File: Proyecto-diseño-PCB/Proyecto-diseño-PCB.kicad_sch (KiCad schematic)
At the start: 41 parts, among them J1 USB_B_Micro, J2 PROGRAMACIÓN/DEPURACIÓN, J3 LADO A, J4 LADO B, SW1 BOTON, SW2 BOTON, SW3 RESET, U1 TPD2EUSB30, U2 LP2950-3.3_TO92, U3 PIC18LF45K50-I/P

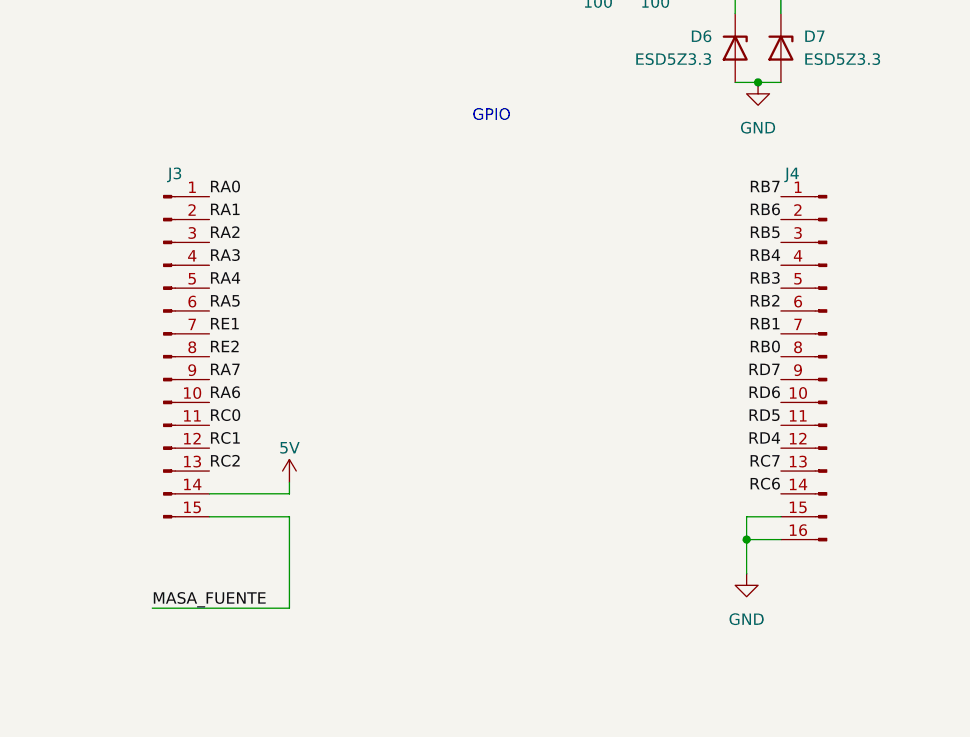
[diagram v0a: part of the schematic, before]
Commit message: Di vuelta pines para que el 1 (cuadrado) sea tierra
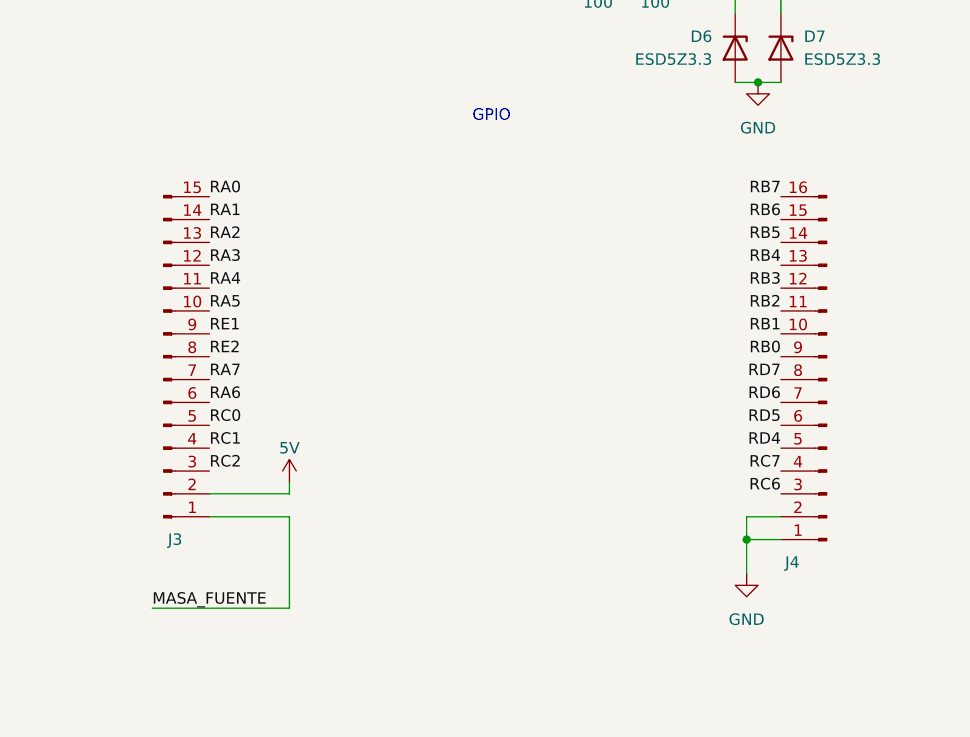
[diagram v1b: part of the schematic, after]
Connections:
- net 5V: now also J3.2 (Pin_2); no longer J3.14 (Pin_14)
- net GND: now also J4.1 (Pin_1), J4.2 (Pin_2); no longer J4.15 (Pin_15), J4.16 (Pin_16)
- net MASA_FUENTE: now also J3.1 (Pin_1); no longer J3.15 (Pin_15)
- net RA0: now also J3.15 (Pin_15); no longer J3.1 (Pin_1)
- net RA1: now also J3.14 (Pin_14); no longer J3.2 (Pin_2)
- net RA2: now also J3.13 (Pin_13); no longer J3.3 (Pin_3)
- net RA3: now also J3.12 (Pin_12); no longer J3.4 (Pin_4)
- net RA4: now also J3.11 (Pin_11); no longer J3.5 (Pin_5)
- net RA5: now also J3.10 (Pin_10); no longer J3.6 (Pin_6)
- net RA6: now also J3.6 (Pin_6); no longer J3.10 (Pin_10)
- net RA7: now also J3.7 (Pin_7); no longer J3.9 (Pin_9)
- net RB0: now also J4.9 (Pin_9); no longer J4.8 (Pin_8)
- net RB1: now also J4.10 (Pin_10); no longer J4.7 (Pin_7)
- net RB2: now also J4.11 (Pin_11); no longer J4.6 (Pin_6)
- net RB3: now also J4.12 (Pin_12); no longer J4.5 (Pin_5)
- net RB4: now also J4.13 (Pin_13); no longer J4.4 (Pin_4)
- net RB5: now also J4.14 (Pin_14); no longer J4.3 (Pin_3)
- net RB6: now also J4.15 (Pin_15); no longer J4.2 (Pin_2)
- net RB7: now also J4.16 (Pin_16); no longer J4.1 (Pin_1)
- net RC0: now also J3.5 (Pin_5); no longer J3.11 (Pin_11)
- net RC1: now also J3.4 (Pin_4); no longer J3.12 (Pin_12)
- net RC2: now also J3.3 (Pin_3); no longer J3.13 (Pin_13)
- net RC6: now also J4.3 (Pin_3); no longer J4.14 (Pin_14)
- net RC7: now also J4.4 (Pin_4); no longer J4.13 (Pin_13)
- net RD4: now also J4.5 (Pin_5); no longer J4.12 (Pin_12)
- net RD5: now also J4.6 (Pin_6); no longer J4.11 (Pin_11)
- net RD6: now also J4.7 (Pin_7); no longer J4.10 (Pin_10)
- net RD7: now also J4.8 (Pin_8); no longer J4.9 (Pin_9)
- net RE1: now also J3.9 (Pin_9); no longer J3.7 (Pin_7)
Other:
- moved on the sheet: J4
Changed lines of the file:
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@@
 	(symbol
 		(lib_id "Connector:Conn_01x16_Pin")
-		(at 270.51 119.38 0)
-		(mirror y)
+		(at 270.51 121.92 180)
 		(unit 1)
 		(exclude_from_sim no)
@@
 		(dnp no)
 		(property "Reference" "J4"
-			(at 266.7 99.06 0)
+			(at 266.7 142.24 0)
 			(effects
 				(font
@@
 		)
 		(property "Value" "LADO B"
-			(at 271.78 120.6499 0)
+			(at 271.78 120.6501 0)
 			(effects
 				(font
@@
 		)
 		(property "Footprint" "Connector_PinHeader_2.54mm:PinHeader_1x16_P2.54mm_Vertical"
-			(at 270.51 119.38 0)
+			(at 270.51 121.92 0)
 			(effects
 				(font
@@
 		)
 		(property "Datasheet" "~"
-			(at 270.51 119.38 0)
+			(at 270.51 121.92 0)
 			(effects
 				(font
@@
 		)
 		(property "Description" "Generic connector, single row, 01x16, script generated"
-			(at 270.51 119.38 0)
+			(at 270.51 121.92 0)
 			(effects
 				(font
@@
 		(lib_id "Connector:Conn_01x15_Pin")
 		(at 196.85 119.38 0)
+		(mirror x)
 		(unit 1)
 		(exclude_from_sim no)
@@
 		(dnp no)
 		(property "Reference" "J3"
-			(at 198.12 99.06 0)
+			(at 198.12 139.7 0)
 			(effects
 				(font
@@
 		)
 		(property "Value" "LADO A"
-			(at 197.485 101.6 0)
-			(effects
-				(font
+			(at 197.485 137.16 0)
+			(effects
+				(font

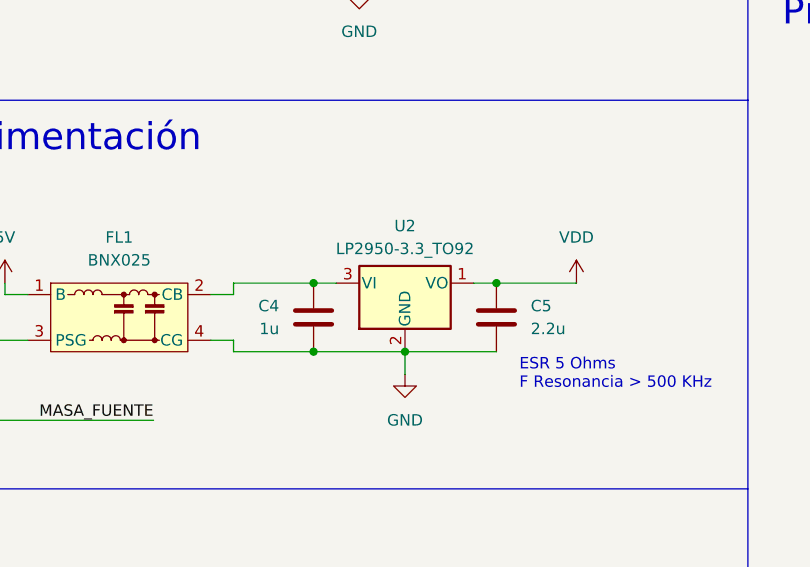
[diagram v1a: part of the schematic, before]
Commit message: Cambié algunos footprints y componentes
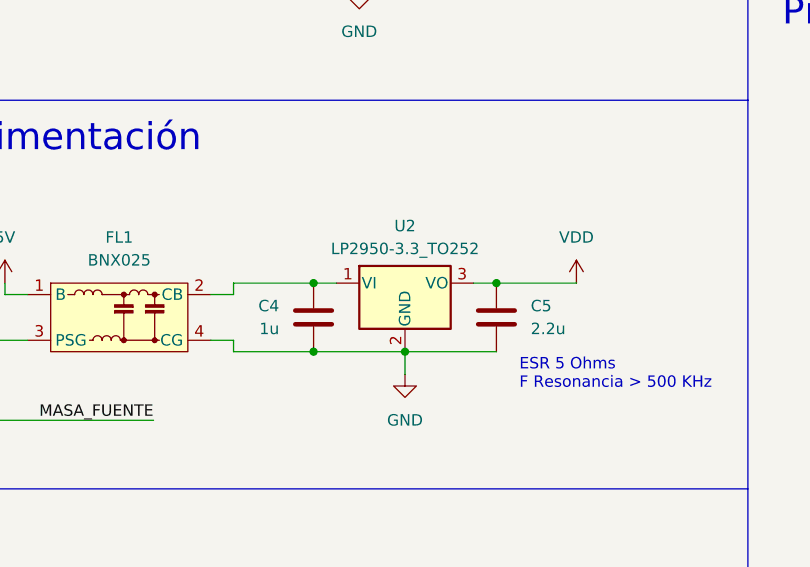
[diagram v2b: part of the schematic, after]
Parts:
- J2: footprint Connector_PinHeader_2.54mm:PinHeader_1x05_P2.54mm_Vertical -> Connector_PinSocket_2.54mm:PinSocket_1x05_P2.54mm_Vertical
- J3: footprint Connector_PinHeader_2.54mm:PinHeader_1x15_P2.54mm_Vertical -> Connector_PinSocket_2.54mm:PinSocket_1x15_P2.54mm_Vertical
- J4: footprint Connector_PinHeader_2.54mm:PinHeader_1x16_P2.54mm_Vertical -> Connector_PinSocket_2.54mm:PinSocket_1x16_P2.54mm_Vertical
- SW3: footprint Button_Switch_THT:SW_PUSH_6mm -> Button_Switch_THT:SW_Tactile_SPST_Angled_PTS645Vx31-2LFS
- U2: value LP2950-3.3_TO92 -> LP2950-3.3_TO252; footprint Package_TO_SOT_THT:TO-92_Inline -> Package_TO_SOT_SMD:TO-252-2; symbol Regulator_Linear:LP2950-3.3_TO92 -> Regulator_Linear:LP2950-3.3_TO252
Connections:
- net VDD: now also U2.3 (VO); no longer U2.1 (VO)
- net at C4.2, FL1.2 (CB): now also U2.1 (VI); no longer U2.3 (VI)
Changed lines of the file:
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@@
 			)
 		)
-		(property "Footprint" "Connector_PinHeader_2.54mm:PinHeader_1x05_P2.54mm_Vertical"
+		(property "Footprint" "Connector_PinSocket_2.54mm:PinSocket_1x05_P2.54mm_Vertical"
 			(at 236.22 69.85 0)
 			(effects
@@
 			)
 		)
-		(property "Footprint" "Button_Switch_THT:SW_PUSH_6mm"
+		(property "Footprint" "Button_Switch_THT:SW_Tactile_SPST_Angled_PTS645Vx31-2LFS"
 			(at 25.4 44.45 0)
 			(effects
@@
 			)
 		)
-		(property "Footprint" "Connector_PinHeader_2.54mm:PinHeader_1x16_P2.54mm_Vertical"
+		(property "Footprint" "Connector_PinSocket_2.54mm:PinSocket_1x16_P2.54mm_Vertical"
 			(at 270.51 121.92 0)
 			(effects
@@
 	)
 	(symbol
-		(lib_id "Regulator_Linear:LP2950-3.3_TO92")
+		(lib_id "Regulator_Linear:LP2950-3.3_TO252")
 		(at 139.7 87.63 0)
 		(unit 1)
@@
 			)
 		)
-		(property "Value" "LP2950-3.3_TO92"
+		(property "Value" "LP2950-3.3_TO252"
 			(at 139.7 83.82 0)
 			(effects
@@
 			)
 		)
-		(property "Footprint" "Package_TO_SOT_THT:TO-92_Inline"
+		(property "Footprint" "Package_TO_SOT_SMD:TO-252-2"
 			(at 139.7 81.915 0)
 			(effects
@@
 			)
 		)
-		(property "Description" "Positive 100mA 30V Linear Micropower Voltage Regulator, Fixed Output 3.3V, TO-92"
+		(property "Description" "Positive 100mA 30V Linear Micropower Voltage Regulator, Fixed Output 3.3V, TO-252"
 			(at 139.7 87.63 0)
 			(effects
@@
 			)
 		)
-		(property "Footprint" "Connector_PinHeader_2.54mm:PinHeader_1x15_P2.54mm_Vertical"
+		(property "Footprint" "Connector_PinSocket_2.54mm:PinSocket_1x15_P2.54mm_Vertical"
 			(at 196.85 119.38 0)
 			(effects

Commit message: rest of the f-ing owl
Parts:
- C1, C2, C3, C4, C5, C6, C7, C8: footprint Capacitor_THT:C_Disc_D3.4mm_W2.1mm_P2.50mm -> Capacitor_SMD:C_1206_3216Metric_Pad1.33x1.80mm_HandSolder
- J3: footprint Connector_PinSocket_2.54mm:PinSocket_1x15_P2.54mm_Vertical -> Connector_PinSocket_2.54mm:PinSocket_1x16_P2.54mm_Vertical; symbol Connector:Conn_01x15_Pin -> Connector:Conn_01x16_Pin
- J4: footprint Connector_PinSocket_2.54mm:PinSocket_1x16_P2.54mm_Vertical -> Connector_PinSocket_2.54mm:PinSocket_1x14_P2.54mm_Vertical; symbol Connector:Conn_01x16_Pin -> Connector:Conn_01x14_Pin
- R1, R10, R11, R12, R13, R2, R3, R4, R5, R6, R7, R8, R9: footprint Resistor_THT:R_Axial_DIN0204_L3.6mm_D1.6mm_P5.08mm_Horizontal -> Resistor_SMD:R_1206_3216Metric_Pad1.30x1.75mm_HandSolder
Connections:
- net BOTON1: now also U3.19 (RD0); no longer U3.22 (RD3)
- net BOTON2: now also U3.20 (RD1); no longer U3.21 (RD2)
- net LED_ROJO: now also U3.22 (RD3); no longer U3.19 (RD0)
- net LED_VERDE: now also U3.21 (RD2); no longer U3.20 (RD1)
- net RA0: now also J3.16 (Pin_16); no longer J3.15 (Pin_15)
- net RA1: now also J3.15 (Pin_15); no longer J3.14 (Pin_14)
- net RA2: now also J3.14 (Pin_14); no longer J3.13 (Pin_13)
- net RA3: now also J3.13 (Pin_13); no longer J3.12 (Pin_12)
- net RA4: now also J3.12 (Pin_12); no longer J3.11 (Pin_11)
- net RA5: now also J3.11 (Pin_11); no longer J3.10 (Pin_10)
- net RE0: now also J3.10 (Pin_10)
- net VI: now reaches C4.2, FL1.2 (CB), U2.1 (VI)
- removed net RB6: J4.15 (Pin_15)
- removed net RB7: J4.16 (Pin_16)
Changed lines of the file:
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@@
 	)
 	(junction
-		(at 255.27 25.4)
-		(diameter 0)
-		(color 0 0 0 0)
-	)
-	(junction
 		(at 139.7 95.25)
 		(diameter 0)
@@
 	(wire
 		(pts
-			(xy 252.73 25.4) (xy 255.27 25.4)
-		)
-		(stroke
-			(width 0)
-			(type default)
-		)
-	)
-	(wire
-		(pts
 			(xy 134.62 53.34) (xy 134.62 54.61)
 		)
@@
 		)
 	)
+	(label "RE0"
+		(at 201.93 114.3 0)
+		(effects
+			(font
+				(size 1.27 1.27)
+			)
+			(justify left bottom)
+		)
+	)
 	(label "RC6"
 		(at 125.73 166.37 180)
@@
 	)
 	(label "RA2"
-		(at 201.93 106.68 0)
+		(at 201.93 104.14 0)
 		(effects
 			(font
@@
 		)
 	)
-	(label "RB7"
-		(at 265.43 101.6 180)
-		(effects
-			(font
-				(size 1.27 1.27)
-			)
-			(justify right bottom)
-		)
-	)
 	(label "RD5"
 		(at 265.43 127 180)
@@
 	)
 	(label "RA0"
-		(at 201.93 101.6 0)
+		(at 201.93 99.06 0)
 		(effects
 			(font
@@
 	)
 	(label "BOTON1"
-		(at 129.54 173.99 180)
+		(at 53.34 173.99 0)
 		(effects
 			(font
 				(size 1.27 1.27)
 			)
-			(justify right bottom)
+			(justify left bottom)
 		)
 	)
@@
 	)
 	(label "LED_ROJO"
-		(at 53.34 173.99 0)
+		(at 129.54 173.99 180)
 		(effects
 			(font
 				(size 1.27 1.27)
 			)
-			(justify left bottom)
+			(justify right bottom)
 		)
 	)
@@
 	)
 	(label "RA3"
-		(at 201.93 109.22 0)
+		(at 201.93 106.68 0)
 		(effects
 			(font
@@
 	)
 	(label "LED_VERDE"
-		(at 53.34 176.53 0)
+		(at 129.54 176.53 180)
 		(effects
 			(font
 				(size 1.27 1.27)
 			)
-			(justify left bottom)
+			(justify right bottom)
 		)
 	)
@@
 	)
 	(label "RA5"
-		(at 201.93 114.3 0)
+		(at 201.93 111.76 0)
 		(effects
 			(font
@@
 		)
 	)
+	(label "VI"
+		(at 123.19 87.63 0)
+		(effects
+			(font
+				(size 1.27 1.27)
+			)
+			(justify left bottom)
+		)
+	)
 	(label "PGD"
 		(at 265.43 72.39 180)
@@
 	)
 	(label "BOTON2"
-		(at 129.54 176.53 180)
+		(at 53.34 176.53 0)
 		(effects
 			(font
 				(size 1.27 1.27)
 			)
-			(justify right bottom)
+			(justify left bottom)
 		)
 	)
@@
 	)
 	(label "RA1"
-		(at 201.93 104.14 0)
+		(at 201.93 101.6 0)
 		(effects
 			(font
@@
 	)
 	(label "RA4"
-		(at 201.93 111.76 0)
+		(at 201.93 109.22 0)
 		(effects
 			(font
@@
 		)
 	)
-	(label "RB6"
-		(at 265.43 104.14 180)
-		(effects
-			(font
-				(size 1.27 1.27)
-			)
-			(justify right bottom)
-		)
-	)
-	(netclass_flag ""
-		(length 2.54)
-		(shape round)
-		(at 252.73 25.4 0)
-		(fields_autoplaced yes)
-		(effects
-			(font
-				(size 1.27 1.27)
-			)
-			(justify left bottom)
-		)
-		(property "Netclass" "Power"
-			(at 253.4285 22.86 0)
-			(effects
-				(font
-					(size 1.27 1.27)
-				)
-				(justify left)
-				(hide yes)
-			)
-		)
-		(property "Component Class" ""
-			(at -83.185 -10.16 0)
-			(effects
-				(font
-					(size 1.27 1.27)
-					(italic yes)
-				)
-			)
-		)
-	)
 	(symbol
 		(lib_id "Device:LED")
@@
 			)
 		)
-		(property "Footprint" "Capacitor_THT:C_Disc_D3.4mm_W2.1mm_P2.50mm"
+		(property "Footprint" "Capacitor_SMD:C_1206_3216Metric_Pad1.33x1.80mm_HandSolder"
 			(at 47.2948 148.59 0)
 			(effects
@@
 			)
 		)
-		(property "Footprint" "Capacitor_THT:C_Disc_D3.4mm_W2.1mm_P2.50mm"
+		(property "Footprint" "Capacitor_SMD:C_1206_3216Metric_Pad1.33x1.80mm_HandSolder"
 			(at 110.1852 53.34 0)
 			(effects
@@
 			)
 		)
-		(property "Footprint" "Resistor_THT:R_Axial_DIN0204_L3.6mm_D1.6mm_P5.08mm_Horizontal"
+		(property "Footprint" "Resistor_SMD:R_1206_3216Metric_Pad1.30x1.75mm_HandSolder"
 			(at 48.006 95.504 90)
 			(effects
@@
 			)
 		)
-		(property "Footprint" "Capacitor_THT:C_Disc_D3.4mm_W2.1mm_P2.50mm"
+		(property "Footprint" "Capacitor_SMD:C_1206_3216Metric_Pad1.33x1.80mm_HandSolder"
 			(at 40.3352 55.88 0)
 			(effects
@@
 			)
 		)
-		(property "Footprint" "Capacitor_THT:C_Disc_D3.4mm_W2.1mm_P2.50mm"
+		(property "Footprint" "Capacitor_SMD:C_1206_3216Metric_Pad1.33x1.80mm_HandSolder"
 			(at 135.5852 151.13 0)
 			(effects
@@
 			)
 		)
-		(property "Footprint" "Resistor_THT:R_Axial_DIN0204_L3.6mm_D1.6mm_P5.08mm_Horizontal"
+		(property "Footprint" "Resistor_SMD:R_1206_3216Metric_Pad1.30x1.75mm_HandSolder"
 			(at 38.354 32.004 90)
 			(effects
@@
 			)
 		)
-		(property "Footprint" "Resistor_THT:R_Axial_DIN0204_L3.6mm_D1.6mm_P5.08mm_Horizontal"
+		(property "Footprint" "Resistor_SMD:R_1206_3216Metric_Pad1.30x1.75mm_HandSolder"
 			(at 141.224 42.164 90)
 			(effects
@@
 			)
 		)
-		(property "Footprint" "Resistor_THT:R_Axial_DIN0204_L3.6mm_D1.6mm_P5.08mm_Horizontal"
+		(property "Footprint" "Resistor_SMD:R_1206_3216Metric_Pad1.30x1.75mm_HandSolder"
 			(at 42.926 129.286 90)
 			(effects
@@
 			)
 		)
-		(property "Footprint" "Resistor_THT:R_Axial_DIN0204_L3.6mm_D1.6mm_P5.08mm_Horizontal"
+		(property "Footprint" "Resistor_SMD:R_1206_3216Metric_Pad1.30x1.75mm_HandSolder"
 			(at 245.364 29.464 90)
 			(effects
@@
 			)
 		)
-		(property "Footprint" "Capacitor_THT:C_Disc_D3.4mm_W2.1mm_P2.50mm"
+		(property "Footprint" "Capacitor_SMD:C_1206_3216Metric_Pad1.33x1.80mm_HandSolder"
 			(at 130.5052 87.63 0)
 			(effects
@@
 			)
 		)
-		(property "Footprint" "Resistor_THT:R_Axial_DIN0204_L3.6mm_D1.6mm_P5.08mm_Horizontal"
+		(property "Footprint" "Resistor_SMD:R_1206_3216Metric_Pad1.30x1.75mm_HandSolder"
 			(at 245.364 73.914 90)
 			(effects
@@
 			)
 		)
-		(property "Footprint" "Resistor_THT:R_Axial_DIN0204_L3.6mm_D1.6mm_P5.08mm_Horizontal"
+		(property "Footprint" "Resistor_SMD:R_1206_3216Metric_Pad1.30x1.75mm_HandSolder"
 			(at 251.714 71.374 90)
 			(effects
@@
 			)
 		)
-		(property "Footprint" "Resistor_THT:R_Axial_DIN0204_L3.6mm_D1.6mm_P5.08mm_Horizontal"
+		(property "Footprint" "Resistor_SMD:R_1206_3216Metric_Pad1.30x1.75mm_HandSolder"
 			(at 251.714 32.004 90)
 			(effects
@@
 			)
 		)
-		(property "Footprint" "Resistor_THT:R_Axial_DIN0204_L3.6mm_D1.6mm_P5.08mm_Horizontal"
+		(property "Footprint" "Resistor_SMD:R_1206_3216Metric_Pad1.30x1.75mm_HandSolder"
 			(at 30.226 95.504 90)
 			(effects
@@
 			)
 		)
-		(property "Footprint" "Capacitor_THT:C_Disc_D3.4mm_W2.1mm_P2.50mm"
+		(property "Footprint" "Capacitor_SMD:C_1206_3216Metric_Pad1.33x1.80mm_HandSolder"
 			(at 150.8252 95.25 0)
 			(effects
@@
 			)
 		)
-		(property "Footprint" "Resistor_THT:R_Axial_DIN0204_L3.6mm_D1.6mm_P5.08mm_Horizontal"
+		(property "Footprint" "Resistor_SMD:R_1206_3216Metric_Pad1.30x1.75mm_HandSolder"
 			(at 83.566 49.784 90)
 			(effects
@@
 			)
 		)
-		(property "Footprint" "Capacitor_THT:C_Disc_D3.4mm_W2.1mm_P2.50mm"
+		(property "Footprint" "Capacitor_SMD:C_1206_3216Metric_Pad1.33x1.80mm_HandSolder"
 			(at 163.5252 53.34 0)
 			(effects
@@
 			)
 		)
-		(property "Footprint" "Resistor_THT:R_Axial_DIN0204_L3.6mm_D1.6mm_P5.08mm_Horizontal"
+		(property "Footprint" "Resistor_SMD:R_1206_3216Metric_Pad1.30x1.75mm_HandSolder"
 			(at 65.786 95.504 90)
 			(effects
@@
 			)
 		)
-		(property "Footprint" "Resistor_THT:R_Axial_DIN0204_L3.6mm_D1.6mm_P5.08mm_Horizontal"
+		(property "Footprint" "Resistor_SMD:R_1206_3216Metric_Pad1.30x1.75mm_HandSolder"
 			(at 135.636 49.784 90)
 			(effects
@@
 	)
 	(symbol
-		(lib_id "Connector:Conn_01x16_Pin")
-		(at 270.51 121.92 180)
+		(lib_id "Connector:Conn_01x14_Pin")
+		(at 270.51 124.46 180)
 		(unit 1)
 		(exclude_from_sim no)
@@
 		(dnp no)
 		(property "Reference" "J4"
-			(at 266.7 142.24 0)
+			(at 266.7 144.78 0)
 			(effects
 				(font
@@
 		)
 		(property "Value" "LADO B"
-			(at 271.78 120.6501 0)
+			(at 271.78 123.1901 0)
 			(effects
 				(font
@@
 			)
 		)
-		(property "Footprint" "Connector_PinSocket_2.54mm:PinSocket_1x16_P2.54mm_Vertical"
-			(at 270.51 121.92 0)
+		(property "Footprint" "Connector_PinSocket_2.54mm:PinSocket_1x14_P2.54mm_Vertical"
+			(at 270.51 124.46 0)
 			(effects
 				(font
@@
 		)
 		(property "Datasheet" "~"
-			(at 270.51 121.92 0)
+			(at 270.51 124.46 0)
 			(effects
 				(font
@@
 			)
 		)
-		(property "Description" "Generic connector, single row, 01x16, script generated"
-			(at 270.51 121.92 0)
+		(property "Description" "Generic connector, single row, 01x14, script generated"
+			(at 270.51 124.46 0)
 			(effects
 				(font
@@
 		(pin "14"
 		)
-		(pin "15"
-		)
-		(pin "16"
-		)
 		(instances
 			(project ""
@@
 			)
 		)
-		(property "Footprint" "Capacitor_THT:C_Disc_D3.4mm_W2.1mm_P2.50mm"
+		(property "Footprint" "Capacitor_SMD:C_1206_3216Metric_Pad1.33x1.80mm_HandSolder"
 			(at 42.2148 171.45 0)
 			(effects
@@
 			)
 		)
-		(property "Footprint" "Resistor_THT:R_Axial_DIN0204_L3.6mm_D1.6mm_P5.08mm_Horizontal"
+		(property "Footprint" "Resistor_SMD:R_1206_3216Metric_Pad1.30x1.75mm_HandSolder"
 			(at 89.154 42.164 90)
 			(effects
@@
 	)
 	(symbol
-		(lib_id "Connector:Conn_01x15_Pin")
+		(lib_id "Connector:Conn_01x16_Pin")
 		(at 196.85 119.38 0)
 		(mirror x)
@@
 			)
 		)
-		(property "Footprint" "Connector_PinSocket_2.54mm:PinSocket_1x15_P2.54mm_Vertical"
+		(property "Footprint" "Connector_PinSocket_2.54mm:PinSocket_1x16_P2.54mm_Vertical"
 			(at 196.85 119.38 0)
 			(effects
@@
 			)
 		)
-		(property "Description" "Generic connector, single row, 01x15, script generated"
+		(property "Description" "Generic connector, single row, 01x16, script generated"
 			(at 196.85 119.38 0)
 			(effects
@@
 		(pin "15"
 		)
+		(pin "16"
+		)
 		(instances
